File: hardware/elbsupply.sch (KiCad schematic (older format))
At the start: 74 parts, among them CON1 AVR-ISP-6, IC1 ATMEGA8-AI, P1 CONN_01X02, Q1 KST2907A, SW1 SW_L, SW2 SW_R, U1 LM393, U2 TPS54331DDA, U3 LT1490, U4 LM358, U5 TS78L05CS, U6 LT3083

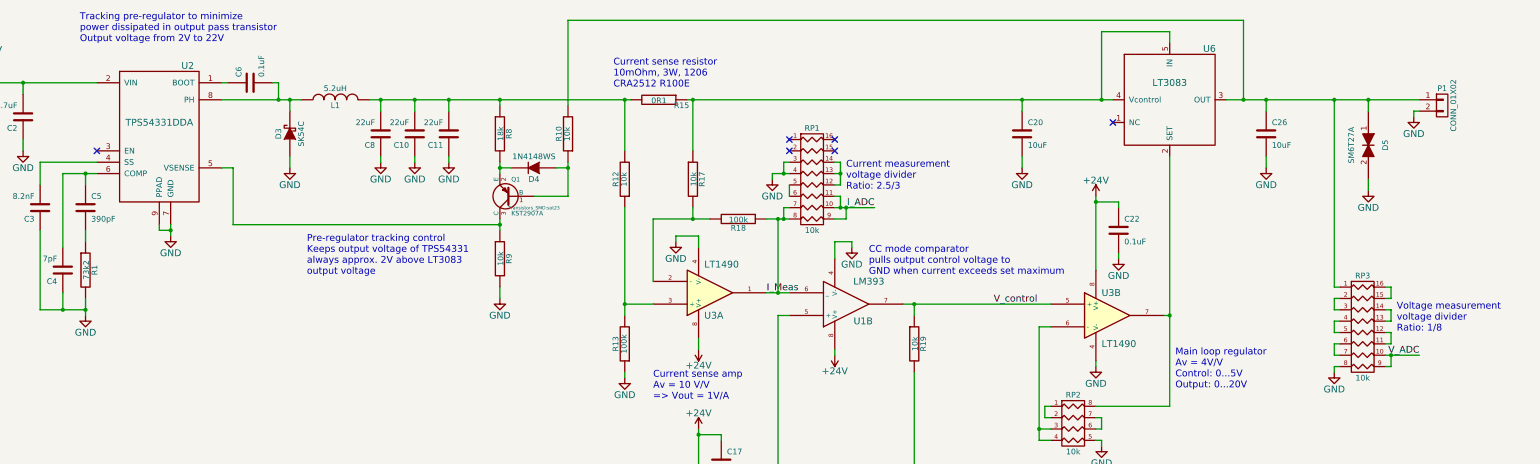
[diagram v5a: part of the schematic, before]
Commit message: slight schematic changes, footprint association almost done
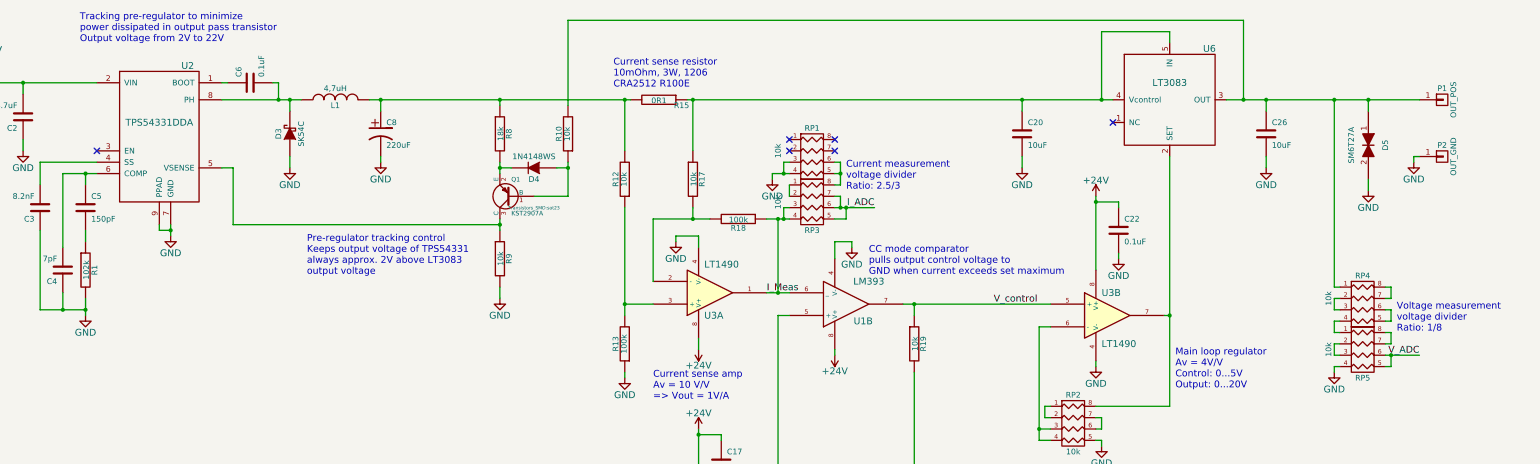
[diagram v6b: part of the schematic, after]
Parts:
- removed C10, C11, C8: 22uF, Capacitors_SMD:C_0805_HandSoldering, symbol C
- removed P1: CONN_01X02, symbol CONN_01X02
- removed RP1, RP3: 10k, symbol R_PACK8
- added C8: 220uF, Capacitors_SMD:c_elec_8x10.5, symbol CP1
- added P1: OUT_POS, symbol CONN_01X01
- added P2: OUT_GND, symbol CONN_01X01
- added RP1, RP3, RP4, RP5: 10k, devthrash_KICAD:YC164-Yageo, symbol R_PACK4
- C1, C12, C13, C14, C15, C16, C17, C18, C19, C2, C20, C21, C22, C23, C24, C25, C26, C27, C3, C4, C6, C7, C9: footprint Capacitors_SMD:C_0805_HandSoldering -> Capacitors_SMD:C_0603_HandSoldering
- C5: value 390pF -> 150pF; footprint Capacitors_SMD:C_0805_HandSoldering -> Capacitors_SMD:C_0603_HandSoldering
- DS1: footprint (none) -> devthrash_KICAD:LCD16X2
- ENC1: footprint (none) -> devthrash_KICAD:ALPS-STEC12E08
- L1: value 5.2uH -> 4,7uH; footprint (none) -> devthrash_KICAD:242418FPS-Fastron
- R1: value 73k2 -> 102k; footprint Resistors_SMD:R_0805_HandSoldering -> Resistors_SMD:R_0603_HandSoldering
- R10, R11, R12, R13, R14, R15, R16, R17, R18, R19, R2, R20, R21, R22, R23, R3, R4, R5, R6, R7, R8, R9: footprint Resistors_SMD:R_0805_HandSoldering -> Resistors_SMD:R_0603_HandSoldering
- RP2: footprint (none) -> devthrash_KICAD:YC164-Yageo
- RV1: footprint (none) -> devthrash_KICAD:BITech-23B
- SW1, SW2: footprint (none) -> devthrash_KICAD:Button-SMT-standard
- U1, U3, U4, U5: footprint Housings_SOIC:SOIC-8_3.9x4.9mm_Pitch1.27mm -> devthrash_KICAD:SO8
- U2: footprint Housings_SOIC:SOIC-8-1EP_3.9x4.9mm_Pitch1.27mm -> devthrash_KICAD:SO8-PowerPAD
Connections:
- net GND: now also C8.2, P2.1 (P1), RP1.3 (P3), RP1.4 (P4), RP5.4 (P4)
- net I_ADC: now also RP3.5 (R4), RP3.6 (R3), RP3.7 (R2)
- net I_Meas: now also RP3.3 (P3), RP3.4 (P4)
- net V_ADC: now also RP5.5 (R4), RP5.6 (R3)
- net at C26.1, D5.1, R10.2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: now also P1.1 (P1), RP4.1 (P1)
- net at L1.2, R12.2, R15.2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: now also C8.1
- new net: RP4.2 (P2), RP4.3 (P3)
- new net: RP4.4 (P4), RP5.1 (P1)
- new net: RP4.5 (R4), RP4.6 (R3)
- new net: RP4.7 (R2), RP4.8 (R1)
- new net: RP5.2 (P2), RP5.3 (P3)
- new net: RP5.7 (R2), RP5.8 (R1)
- new net: RP1.5 (R4), RP1.6 (R3), RP3.8 (R1)
- new net: RP3.1 (P1), RP3.2 (P2)

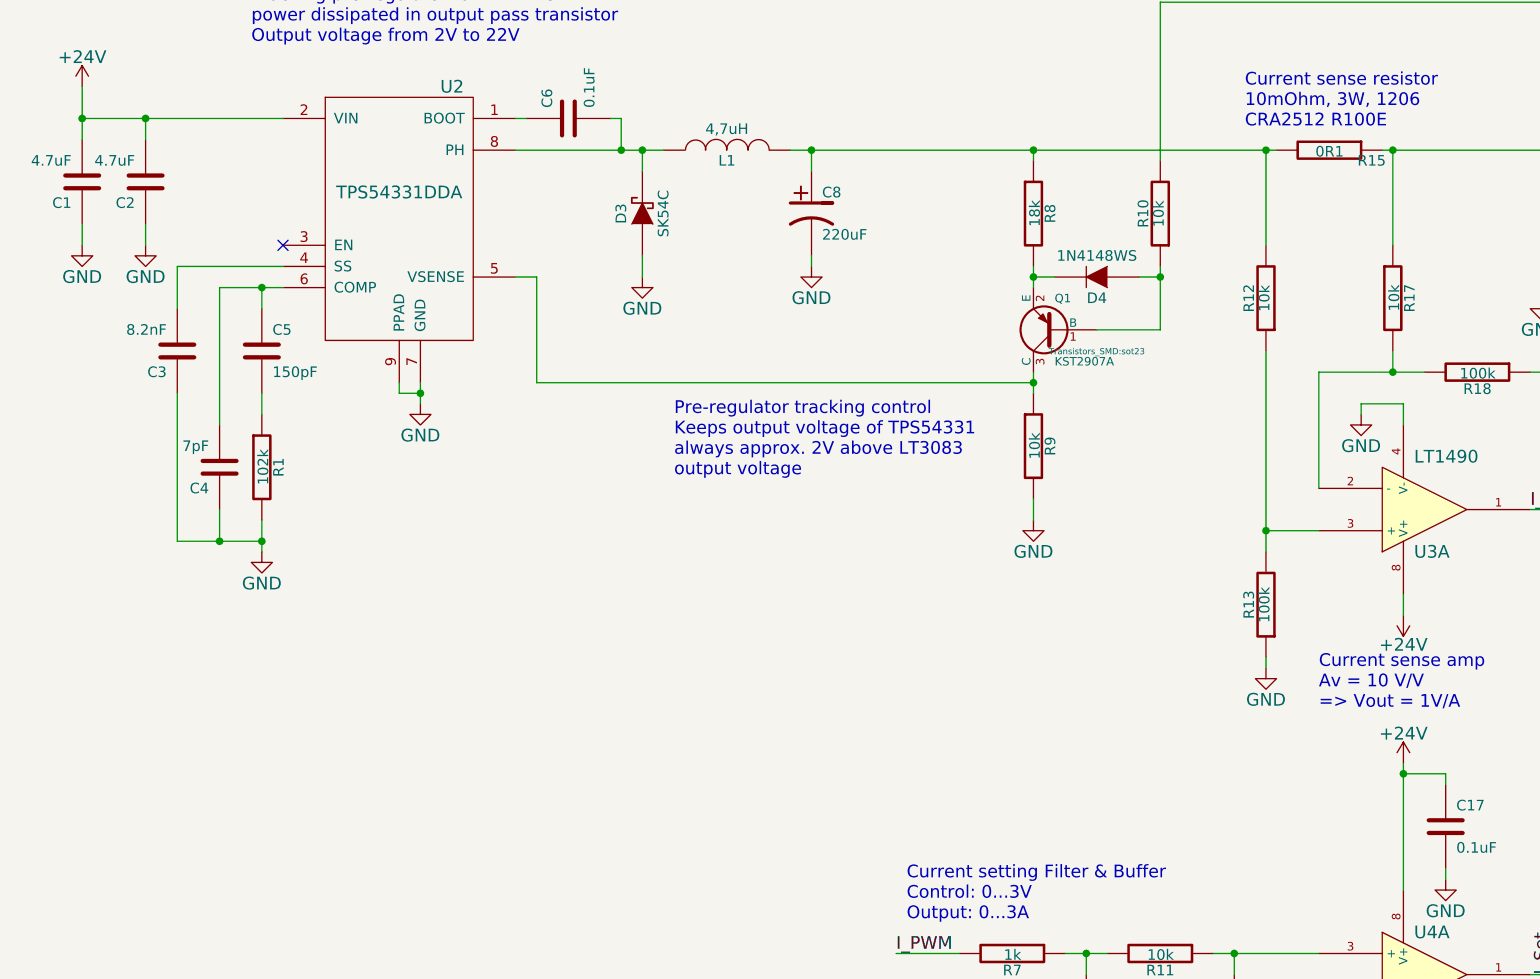
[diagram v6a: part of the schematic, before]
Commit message: added screw terminal power input
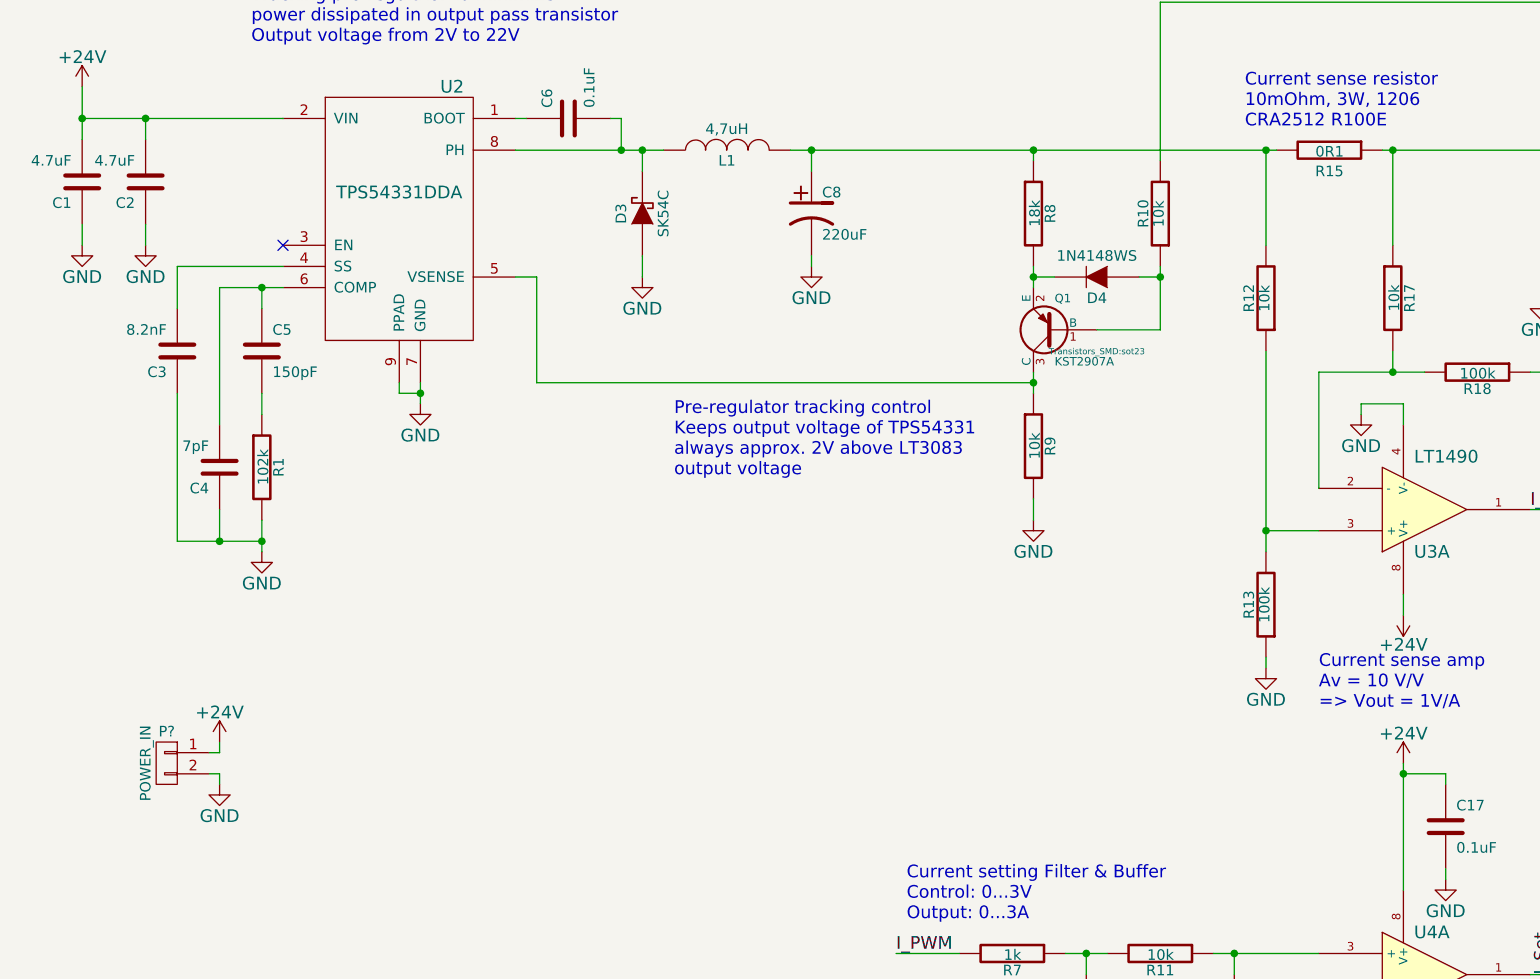
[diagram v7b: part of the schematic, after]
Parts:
- added P?: POWER_IN, symbol CONN_01X02
- P1, P2: footprint (none) -> devthrash_KICAD:SKS-PK10A
- R15: footprint Resistors_SMD:R_0603_HandSoldering -> devthrash_KICAD:CRA2512-Bourns
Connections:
- net +24V: now also P?.1 (P1)
- net GND: now also P?.2 (P2)
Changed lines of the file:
@@
 U 1 1 54F1A4F0
 P 6700 1400
-F 0 "R15" V 6750 1600 50  0000 C CNN
+F 0 "R15" V 6800 1400 50  0000 C CNN
 F 1 "0R1" V 6707 1401 50  0000 C CNN
-F 2 "Resistors_SMD:R_0603_HandSoldering" V 6630 1400 30  0001 C CNN
+F 2 "devthrash_KICAD:CRA2512-Bourns" V 6630 1400 30  0001 C CNN
 F 3 "" H 6700 1400 30  0000 C CNN
 	1    6700 1400
@@
 F 0 "P1" H 13600 1500 50  0000 C CNN
 F 1 "OUT_POS" V 13700 1400 50  0000 C CNN
-F 2 "" H 13600 1400 60  0001 C CNN
+F 2 "devthrash_KICAD:SKS-PK10A" H 13600 1400 60  0001 C CNN
 F 3 "" H 13600 1400 60  0000 C CNN
 	1    13600 1400
@@
 F 0 "P2" H 13600 2000 50  0000 C CNN
 F 1 "OUT_GND" V 13700 1900 50  0000 C CNN
-F 2 "" H 13600 1900 60  0001 C CNN
+F 2 "devthrash_KICAD:SKS-PK10A" H 13600 1900 60  0001 C CNN
 F 3 "" H 13600 1900 60  0000 C CNN
 	1    13600 1900
@@
 	1    0    0    -1
 $EndComp
+$Comp
+L CONN_01X02 P?
+U 1 1 54F749D9
+P 1200 4300
+F 0 "P?" H 1200 4450 50  0000 C CNN
+F 1 "POWER_IN" V 1300 4300 50  0000 C CNN
+F 2 "" H 1200 4300 60  0000 C CNN
+F 3 "" H 1200 4300 60  0000 C CNN
+	1    1200 4300
+	-1   0    0    -1
+$EndComp
+$Comp
+L GND #PWR?
+U 1 1 54F75568
+P 1450 4400
+F 0 "#PWR?" H 1450 4150 60  0001 C CNN
+F 1 "GND" H 1450 4250 60  0000 C CNN
+F 2 "" H 1450 4400 60  0000 C CNN
+F 3 "" H 1450 4400 60  0000 C CNN
+	1    1450 4400
+	1    0    0    -1
+$EndComp
+Wire Wire Line
+	1450 4400 1450 4350
+Wire Wire Line
+	1450 4350 1400 4350
+$Comp
+L +24V #PWR?
+U 1 1 54F7576C
+P 1450 4200
+F 0 "#PWR?" H 1450 4050 60  0001 C CNN
+F 1 "+24V" H 1450 4340 60  0000 C CNN
+F 2 "" H 1450 4200 60  0000 C CNN
+F 3 "" H 1450 4200 60  0000 C CNN
+	1    1450 4200
+	1    0    0    -1
+$EndComp
+Wire Wire Line
+	1450 4200 1450 4250
+Wire Wire Line
+	1450 4250 1400 4250
 $EndSCHEMATC

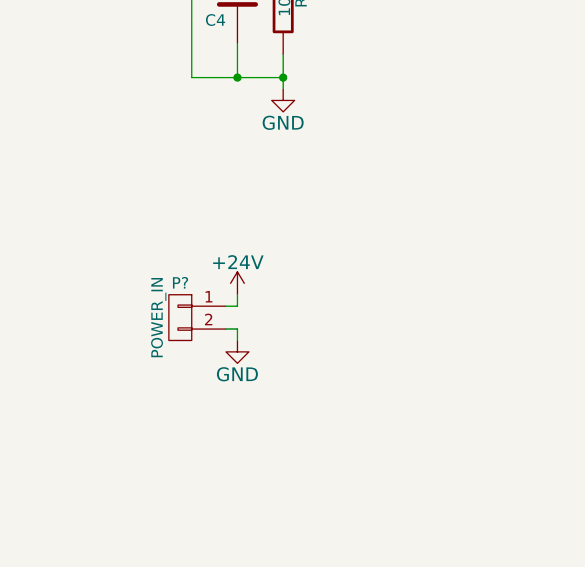
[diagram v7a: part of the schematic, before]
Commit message: binding post distance is now 3/4 inch
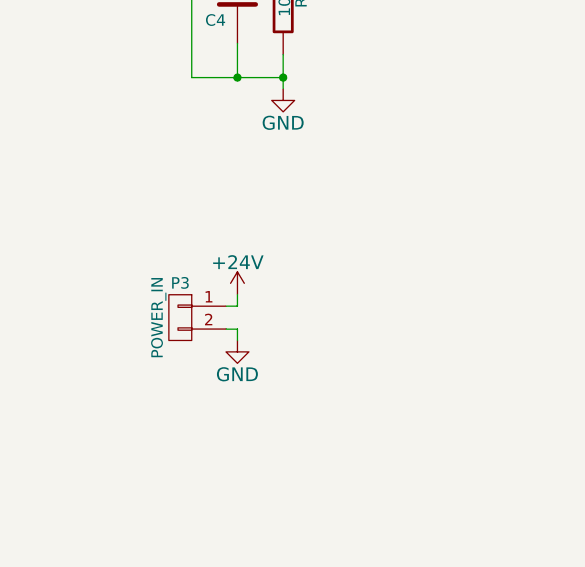
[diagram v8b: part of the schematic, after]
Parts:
- P3: renamed from P?; footprint (none) -> Connect:bornier2
